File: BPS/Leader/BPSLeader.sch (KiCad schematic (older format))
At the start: 22 parts, among them J1 GPIO Analyzer, J2 SPI Analyzer, J3 CAN Analyzer, J4 SWD, SW1 B3SL-1002P, U1 STM32F413RHTx, Y1 8M

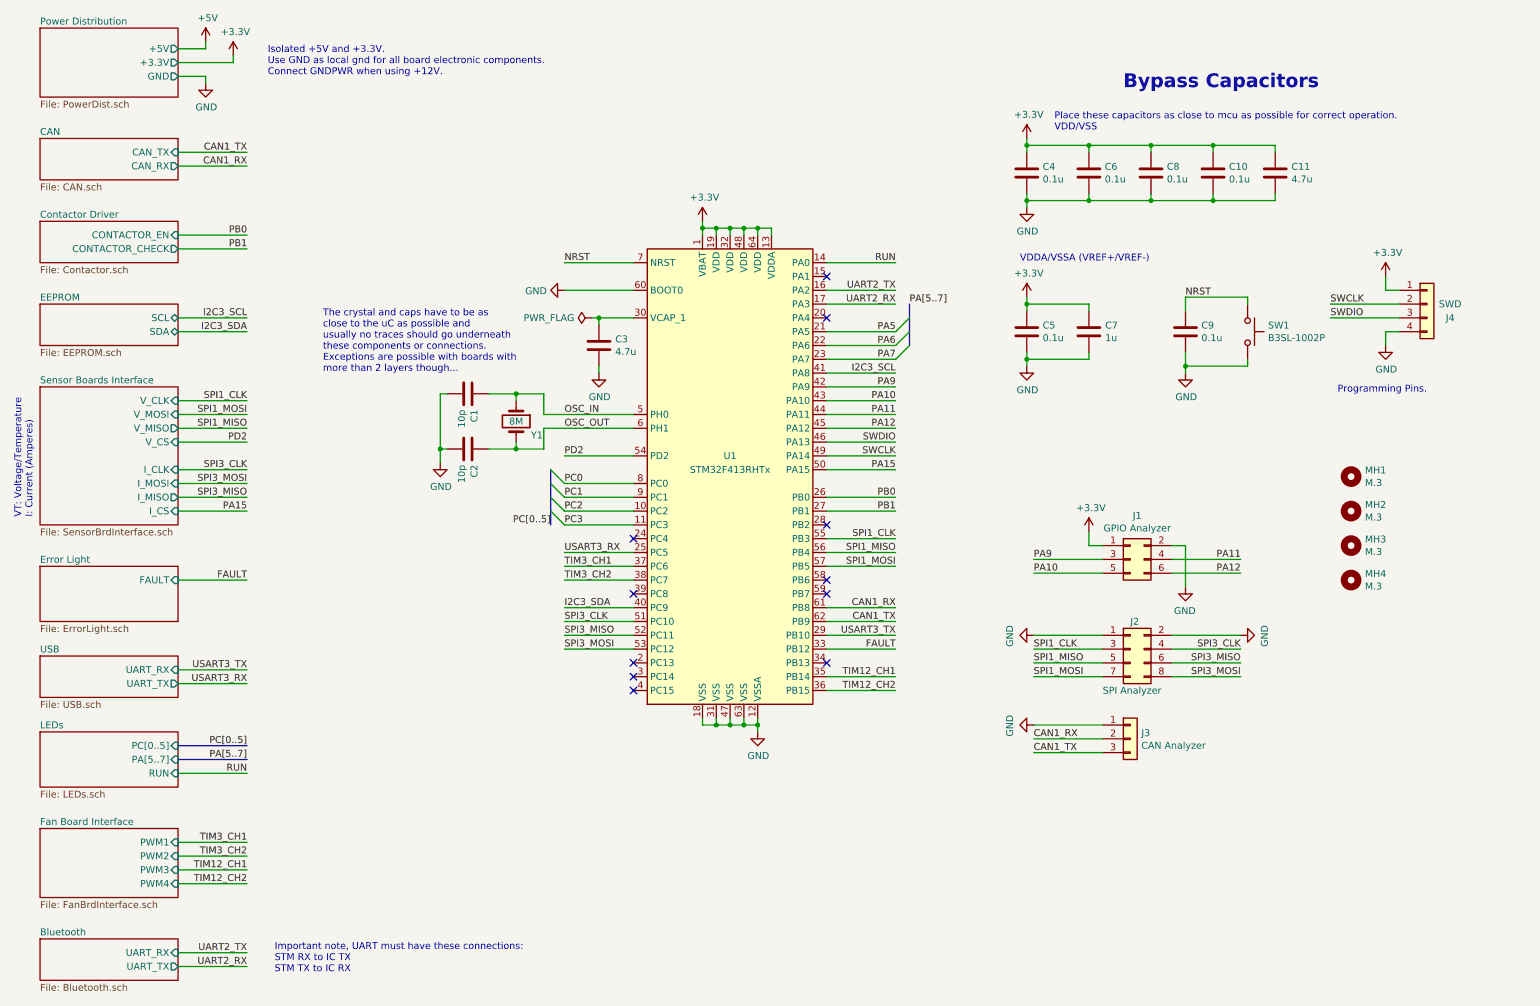
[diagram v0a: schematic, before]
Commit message: Places most components of leader board in their respective locations with nothing traced
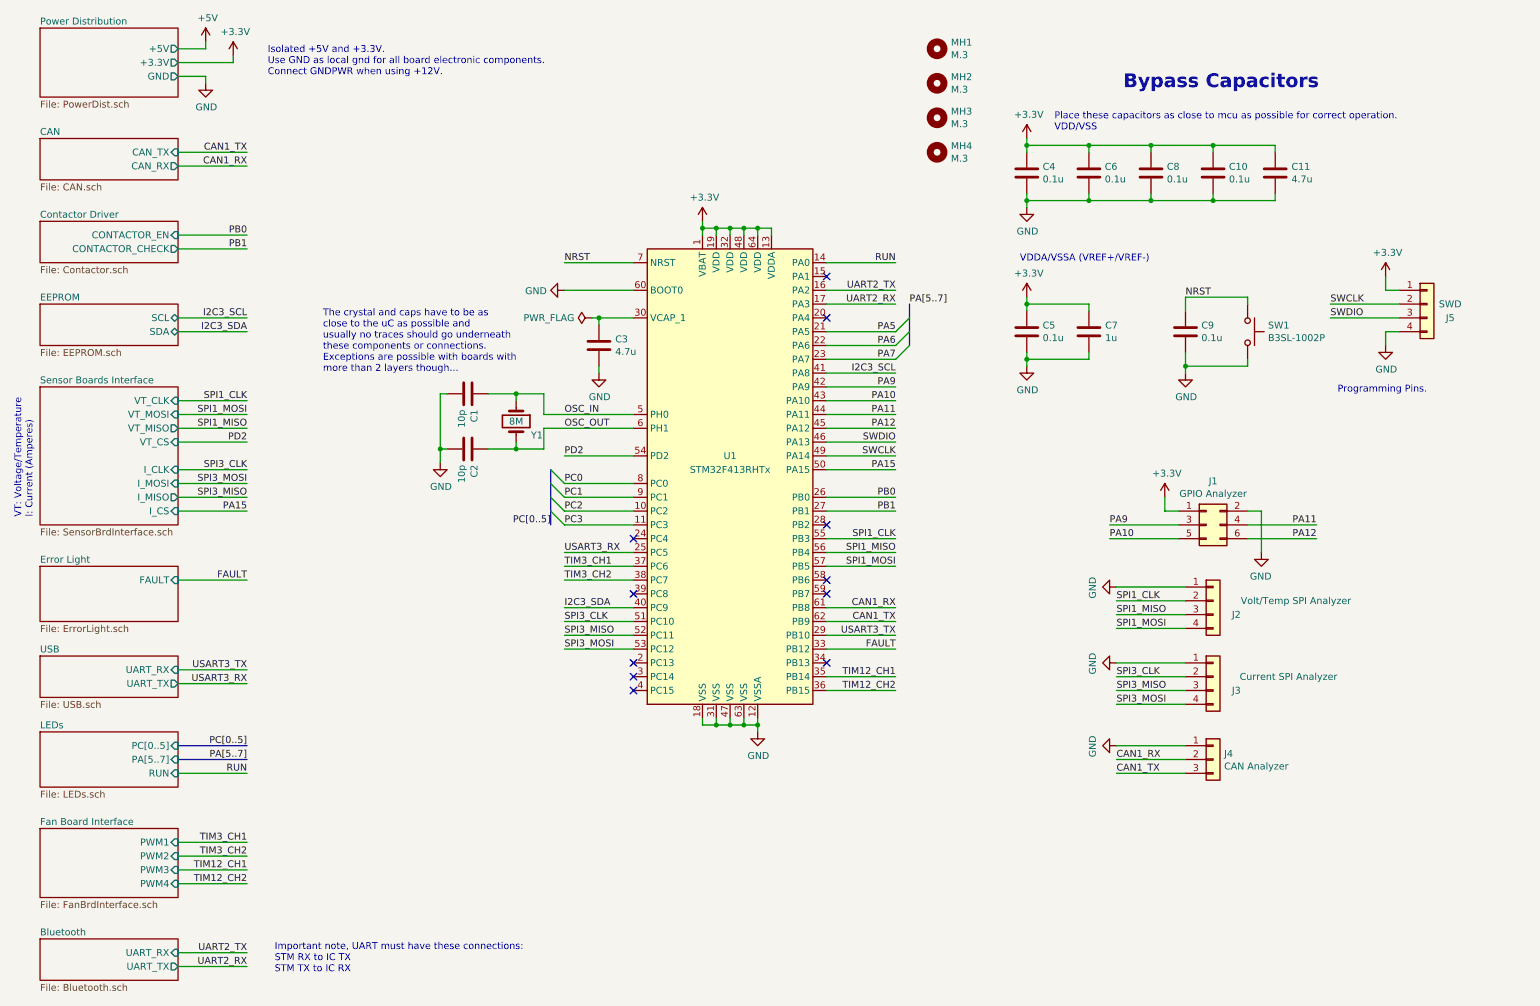
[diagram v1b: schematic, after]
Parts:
- removed J2: SPI Analyzer, Connector_PinHeader_2.54mm:PinHeader_2x04_P2.54mm_Vertical, symbol Connector_Generic:Conn_02x04_Odd_Even
- added J2: Volt/Temp SPI Analyzer, Connector_PinHeader_2.54mm:PinHeader_1x04_P2.54mm_Vertical, symbol Connector_Generic:Conn_01x04
- added J3: Current SPI Analyzer, Connector_PinHeader_2.54mm:PinHeader_1x04_P2.54mm_Vertical, symbol Connector_Generic:Conn_01x04
- renumbered J3 to J4, J4 to J5
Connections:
- net GND: now also J2.1 (Pin_1), J3.1 (Pin_1)
- net SPI1_CLK: now also J2.2 (Pin_2)
- net SPI1_MISO: now also J2.3 (Pin_3)
- net SPI1_MOSI: now also J2.4 (Pin_4)
- net SPI3_CLK: now also J3.2 (Pin_2)
- net SPI3_MISO: now also J3.3 (Pin_3)
- net SPI3_MOSI: now also J3.4 (Pin_4)
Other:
- moved on the sheet: J1, J4, MH1, MH2, MH3, MH4

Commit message: Adds power planes
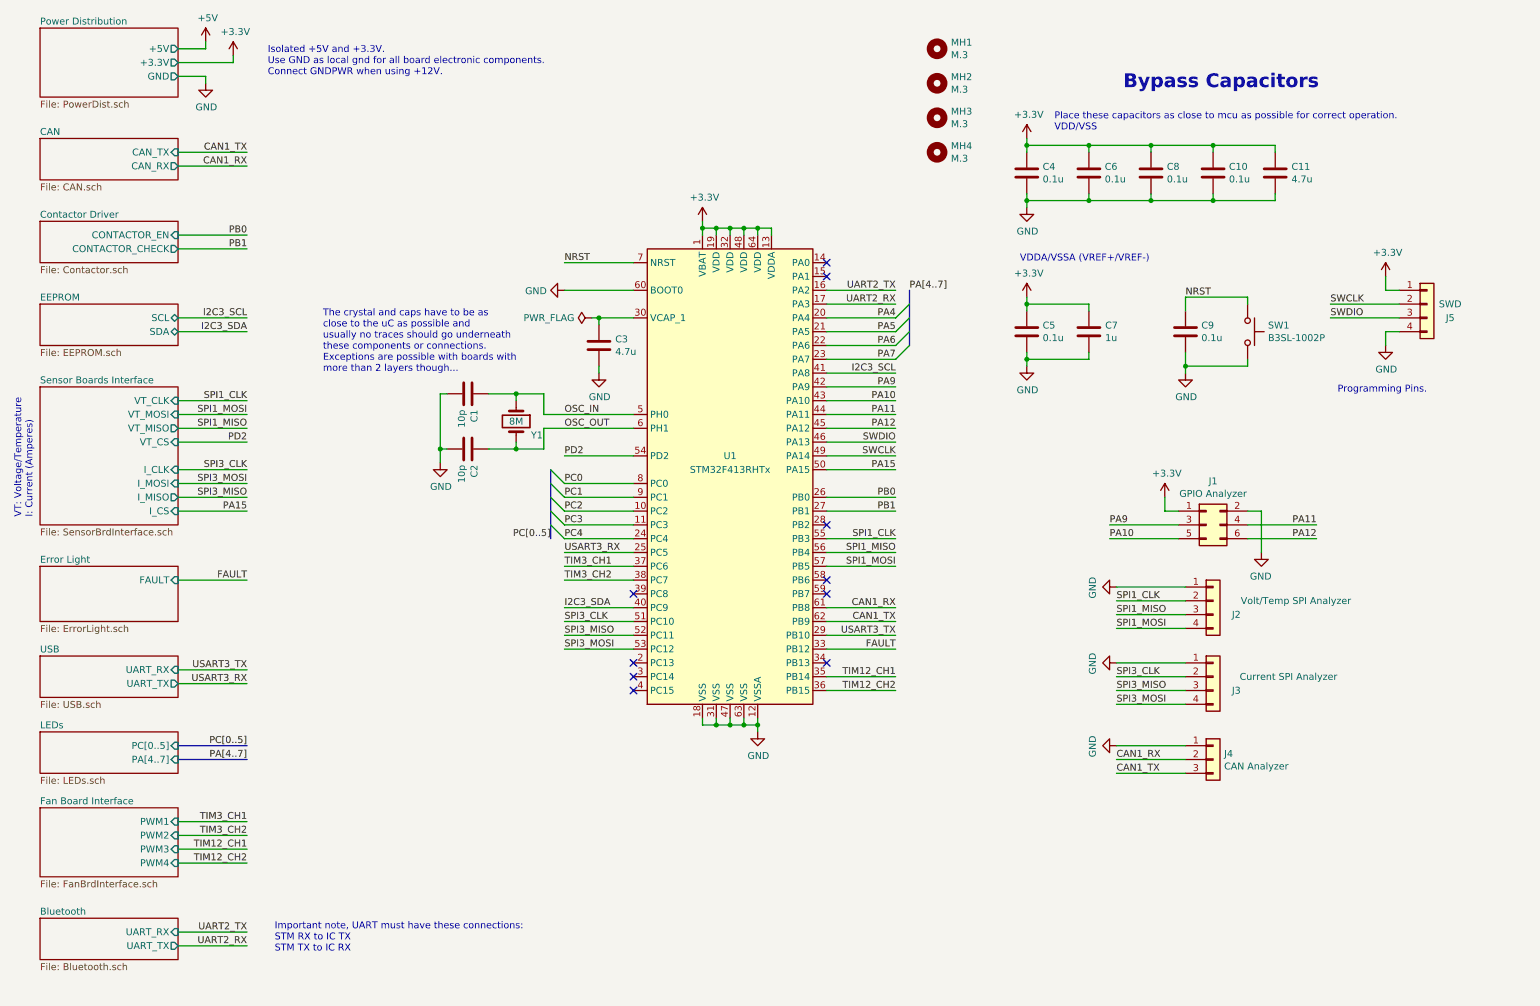
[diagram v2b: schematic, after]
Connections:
- net PA4: now reaches U1.20 (PA4)
- net PC4: now reaches U1.24 (PC4)
- net RUN: no longer names the net of U1.14 (PA0)
- no-connect marks 11 -> 10
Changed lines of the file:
@@
 	10550 2900 10650 2900
 $Sheet
-S 800  5800 1000 400
+S 800  5800 1000 300
 U 5C392C6A
 F0 "LEDs" 50
 F1 "LEDs.sch" 50
 F2 "PC[0..5]" I R 1800 5900 50
-F3 "PA[5..7]" I R 1800 6000 50
-F4 "RUN" I R 1800 6100 50
+F3 "PA[4..7]" I R 1800 6000 50
 $EndSheet
 Text Notes 8650 1150 0    100  ~ 20
@@
 Entry Wire Line
 	4500 4000 4600 4100
-Text Label 4500 4300 2    50   ~ 0
+Text Label 4500 4400 2    50   ~ 0
 PC[0..5]
 Text Label 2300 5900 2    50   ~ 0
@@
 Entry Wire Line
 	7000 3000 7100 2900
-Entry Wire Line
-	7000 2900 7100 2800
-Text Label 7100 2700 0    50   ~ 0
-PA[5..7]
+Text Label 7100 2600 0    50   ~ 0
+PA[4..7]
 Wire Bus Line
 	1800 5900 2300 5900
@@
 	1800 6000 2300 6000
 Text Label 2300 6000 2    50   ~ 0
-PA[5..7]
+PA[4..7]
 $Comp
 L Mechanical:MountingHole MH1
@@
 NoConn ~ 5100 5300
 NoConn ~ 6500 4300
-NoConn ~ 6500 2800
 NoConn ~ 6500 2500
 $Comp
@@
 FAULT
 Wire Wire Line
-	6500 2400 7000 2400
-Text Label 7000 2400 2    50   ~ 0
-RUN
-Wire Wire Line
-	1800 6100 2300 6100
-Text Label 2300 6100 2    50   ~ 0
-RUN
+	5100 4400 4600 4400
+Text Label 4600 4400 0    50   ~ 0
+PC4
 Wire Wire Line
 	4250 3350 4250 3400
@@
 	10550 2600 10650 2600
 NoConn ~ 6500 4800
-NoConn ~ 5100 4400
 Wire Wire Line
 	5100 4500 4600 4500
@@
 Wire Wire Line
 	9100 5050 8600 5050
-Text Label 8600 4850 0    50   ~ 0
-SPI1_CLK
 Text Label 8600 4950 0    50   ~ 0
 SPI1_MISO
-Text Label 8600 5050 0    50   ~ 0
-SPI1_MOSI
-$Sheet
-S 800  6500 1000 500
+$Sheet
+S 800  6350 1000 500
 U 5F145F02
 F0 "Fan Board Interface" 50
 F1 "FanBrdInterface.sch" 50
-F2 "PWM1" I R 1800 6600 50
-F3 "PWM2" I R 1800 6700 50
-F4 "PWM3" I R 1800 6800 50
-F5 "PWM4" I R 1800 6900 50
+F2 "PWM1" I R 1800 6450 50
+F3 "PWM2" I R 1800 6550 50
+F4 "PWM3" I R 1800 6650 50
+F5 "PWM4" I R 1800 6750 50
 $EndSheet
 Wire Wire Line
@@
 TIM12_CH2
 Wire Wire Line
-	1800 6600 2300 6600
-Wire Wire Line
-	2300 6700 1800 6700
-Text Label 2300 6600 2    50   ~ 0
+	1800 6450 2300 6450
+Wire Wire Line
+	2300 6550 1800 6550
+Text Label 2300 6450 2    50   ~ 0
 TIM3_CH1
-Text Label 2300 6700 2    50   ~ 0
+Text Label 2300 6550 2    50   ~ 0
 TIM3_CH2
 Wire Wire Line
-	1800 6800 2300 6800
-Wire Wire Line
-	1800 6900 2300 6900
-Text Label 2300 6800 2    50   ~ 0
+	1800 6650 2300 6650
+Wire Wire Line
+	1800 6750 2300 6750
+Text Label 2300 6650 2    50   ~ 0
 TIM12_CH1
-Text Label 2300 6900 2    50   ~ 0
+Text Label 2300 6750 2    50   ~ 0
 TIM12_CH2
 $Sheet
-S 800  7300 1000 300
+S 800  7150 1000 300
 U 5F24B488
 F0 "Bluetooth" 50
 F1 "Bluetooth.sch" 50
-F2 "UART_RX" I R 1800 7400 50
-F3 "UART_TX" O R 1800 7500 50
+F2 "UART_RX" I R 1800 7250 50
+F3 "UART_TX" O R 1800 7350 50
 $EndSheet
 Wire Wire Line
@@
 UART2_RX
 Wire Wire Line
-	1800 7400 2300 7400
-Wire Wire Line
-	2300 7500 1800 7500
-Text Label 2300 7400 2    50   ~ 0
+	1800 7250 2300 7250
+Wire Wire Line
+	2300 7350 1800 7350
+Text Label 2300 7250 2    50   ~ 0
 UART2_TX
-Text Label 2300 7500 2    50   ~ 0
+Text Label 2300 7350 2    50   ~ 0
 UART2_RX
-Text Notes 2500 7550 0    50   ~ 0
+Text Notes 2500 7400 0    50   ~ 0
 Important note, UART must have these connections:\nSTM RX to IC TX\nSTM TX to IC RX
 Wire Wire Line
@@
 Wire Wire Line
 	9100 5600 8600 5600
-Text Label 8600 5600 0    50   ~ 0
-SPI3_MOSI
 Text Label 8600 5500 0    50   ~ 0
 SPI3_MISO
-Text Label 8600 5400 0    50   ~ 0
-SPI3_CLK
 $Comp
 L power:GND #PWR014
@@
 	1    0    0    -1
 $EndComp
+Wire Wire Line
+	6500 2800 7000 2800
+Entry Wire Line
+	7000 2800 7100 2700
+Entry Wire Line
+	7000 2900 7100 2800
+Text Label 7000 2800 2    50   ~ 0
+PA4
+Entry Wire Line
+	4500 4300 4600 4400
+NoConn ~ 6500 2400
 Wire Bus Line
-	7100 2700 7100 3000
+	7100 2600 7100 3000
 Wire Bus Line
-	4500 3900 4500 4300
+	4500 3900 4500 4400
+Text Label 8600 5600 0    50   ~ 0
+SPI3_MOSI
+Text Label 8600 5400 0    50   ~ 0
+SPI3_CLK
+Text Label 8600 4850 0    50   ~ 0
+SPI1_CLK
+Text Label 8600 5050 0    50   ~ 0
+SPI1_MOSI
 $EndSCHEMATC

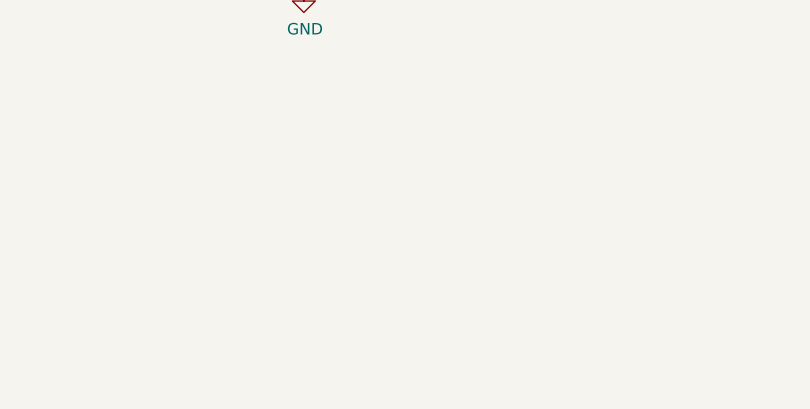
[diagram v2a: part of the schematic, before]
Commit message: Finished leader board
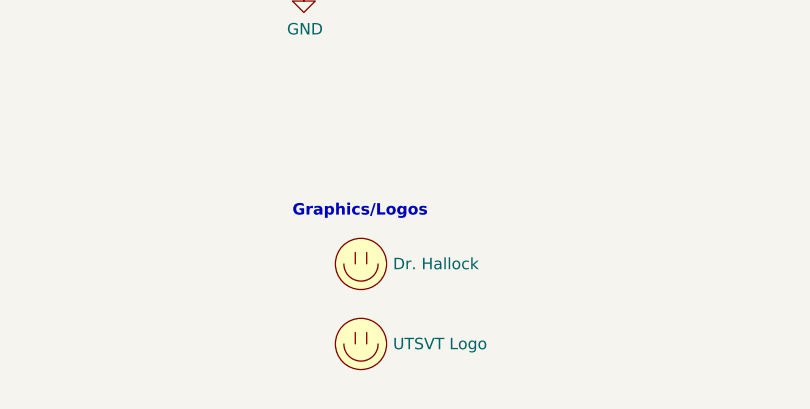
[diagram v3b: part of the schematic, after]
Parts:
- added LOGO2: Dr. Hallock, UTSVT_Special:Hallock_Image_Small, symbol utsvt-misc:Logo_Placeholder
- added LOGO3: UTSVT Logo, UTSVT_Special:UTSVT_Logo_Symbol, symbol utsvt-misc:Logo_Placeholder
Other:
- note added: "Graphics/Logos"
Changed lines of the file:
@@
 	4500 4300 4600 4400
 NoConn ~ 6500 2400
-Wire Bus Line
-	7100 2600 7100 3000
-Wire Bus Line
-	4500 3900 4500 4400
 Text Label 8600 5600 0    50   ~ 0
 SPI3_MOSI
@@
 Text Label 8600 5050 0    50   ~ 0
 SPI1_MOSI
+Text Notes 5950 6800 0    50   ~ 10
+Graphics/Logos
+$Comp
+L utsvt-misc:Logo_Placeholder LOGO2
+U 1 1 5F2CE831
+P 6250 7000
+F 0 "LOGO2" H 6250 7150 50  0001 C CNN
+F 1 "Dr. Hallock" H 6390 7000 50  0000 L CNN
+F 2 "UTSVT_Special:Hallock_Image_Small" H 6250 7075 50  0001 C CNN
+F 3 "" H 6250 7075 50  0001 C CNN
+	1    6250 7000
+	1    0    0    -1
+$EndComp
+$Comp
+L utsvt-misc:Logo_Placeholder LOGO3
+U 1 1 5F2D0A96
+P 6250 7350
+F 0 "LOGO3" H 6250 7500 50  0001 C CNN
+F 1 "UTSVT Logo" H 6390 7350 50  0000 L CNN
+F 2 "UTSVT_Special:UTSVT_Logo_Symbol" H 6250 7425 50  0001 C CNN
+F 3 "" H 6250 7425 50  0001 C CNN
+	1    6250 7350
+	1    0    0    -1
+$EndComp
+Wire Bus Line
+	7100 2600 7100 3000
+Wire Bus Line
+	4500 3900 4500 4400
 $EndSCHEMATC

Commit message: Simplifies dc-dc converter schematics
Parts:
- renumbered LOGO2 to LOGO1, LOGO3 to LOGO2
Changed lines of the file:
@@
 Graphics/Logos
 $Comp
-L utsvt-misc:Logo_Placeholder LOGO2
+L utsvt-misc:Logo_Placeholder LOGO1
 U 1 1 5F2CE831
 P 6250 7000
-F 0 "LOGO2" H 6250 7150 50  0001 C CNN
+F 0 "LOGO1" H 6250 7150 50  0001 C CNN
 F 1 "Dr. Hallock" H 6390 7000 50  0000 L CNN
 F 2 "UTSVT_Special:Hallock_Image_Small" H 6250 7075 50  0001 C CNN
@@
 $EndComp
 $Comp
-L utsvt-misc:Logo_Placeholder LOGO3
+L utsvt-misc:Logo_Placeholder LOGO2
 U 1 1 5F2D0A96
 P 6250 7350
-F 0 "LOGO3" H 6250 7500 50  0001 C CNN
+F 0 "LOGO2" H 6250 7500 50  0001 C CNN
 F 1 "UTSVT Logo" H 6390 7350 50  0000 L CNN
 F 2 "UTSVT_Special:UTSVT_Logo_Symbol" H 6250 7425 50  0001 C CNN
